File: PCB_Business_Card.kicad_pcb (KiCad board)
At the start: 2 copper layers, 88.9 x 50.8 mm, 6 parts, among them U1 NT3H1101W0FTTJ

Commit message: Updated Render
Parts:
- added G***: LOGO, LOGO, F.Cu at (114.1, 89.0)
- added G***: LOGO, LOGO, F.Cu at (161.5, 90.6)
- moved REF** 3.34 mm to (114.1, 89.0)
- moved C1 3.34 mm to (145.6, 90.6)
- moved D1 3.34 mm to (146.5, 93.2)
- moved R1 3.34 mm to (147.3, 90.6)
- moved U1 3.34 mm to (141.1, 89.5)
- moved ? 3.34 mm to (145.9, 88.5)
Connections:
- REF** pad : (no net) -> Net-(U1-LA)
- REF** pad 1: (no net) -> Net-(U1-LA)
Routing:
- net Net-(U1-LA): track 2.55 -> 22.0 mm
- net Net-(D1-K): track 0.00 -> 14.9 mm
- added copper zone on B.Cu, net (none)
- added copper zone on F.Cu, net (none)
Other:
- board text added: "linkedin.com/in/rahim-aziz"
- board text removed: "azizr6@mcmaster.ca"

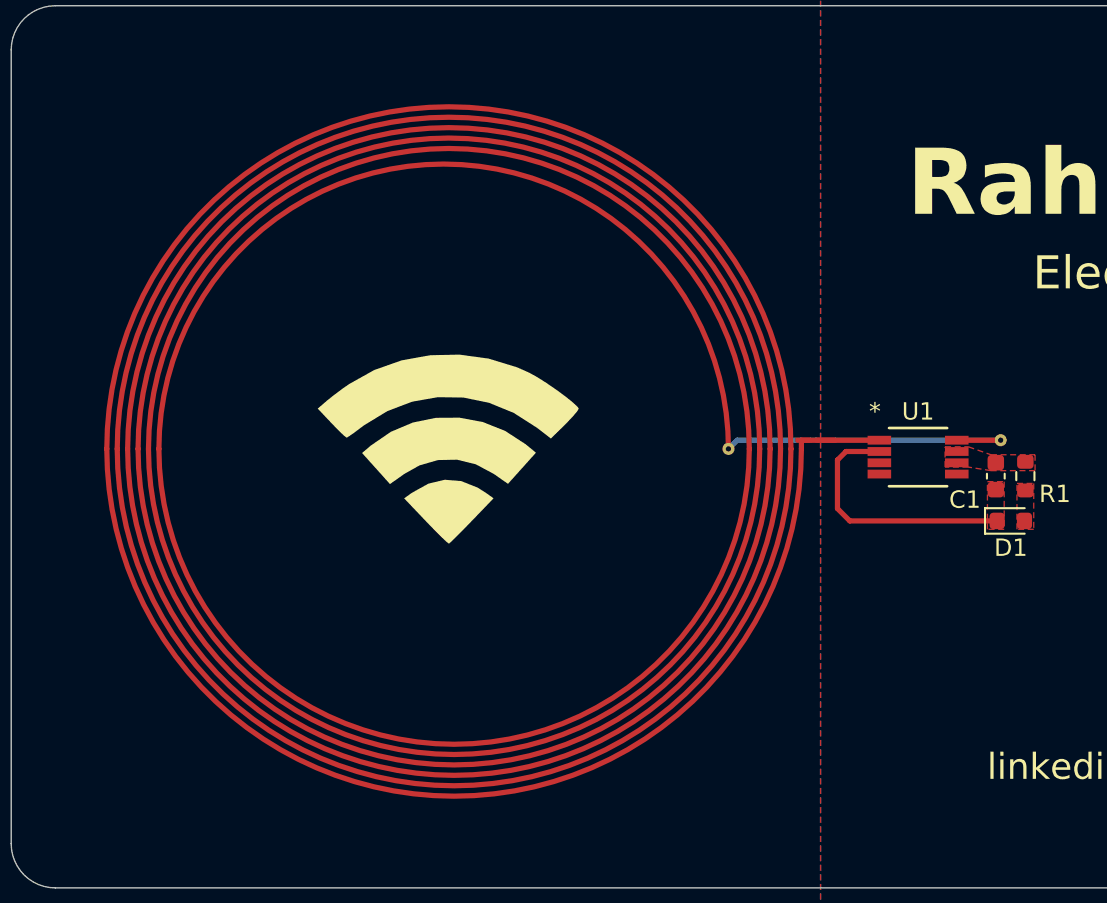
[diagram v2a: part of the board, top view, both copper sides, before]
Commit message: Added tuning capacitor
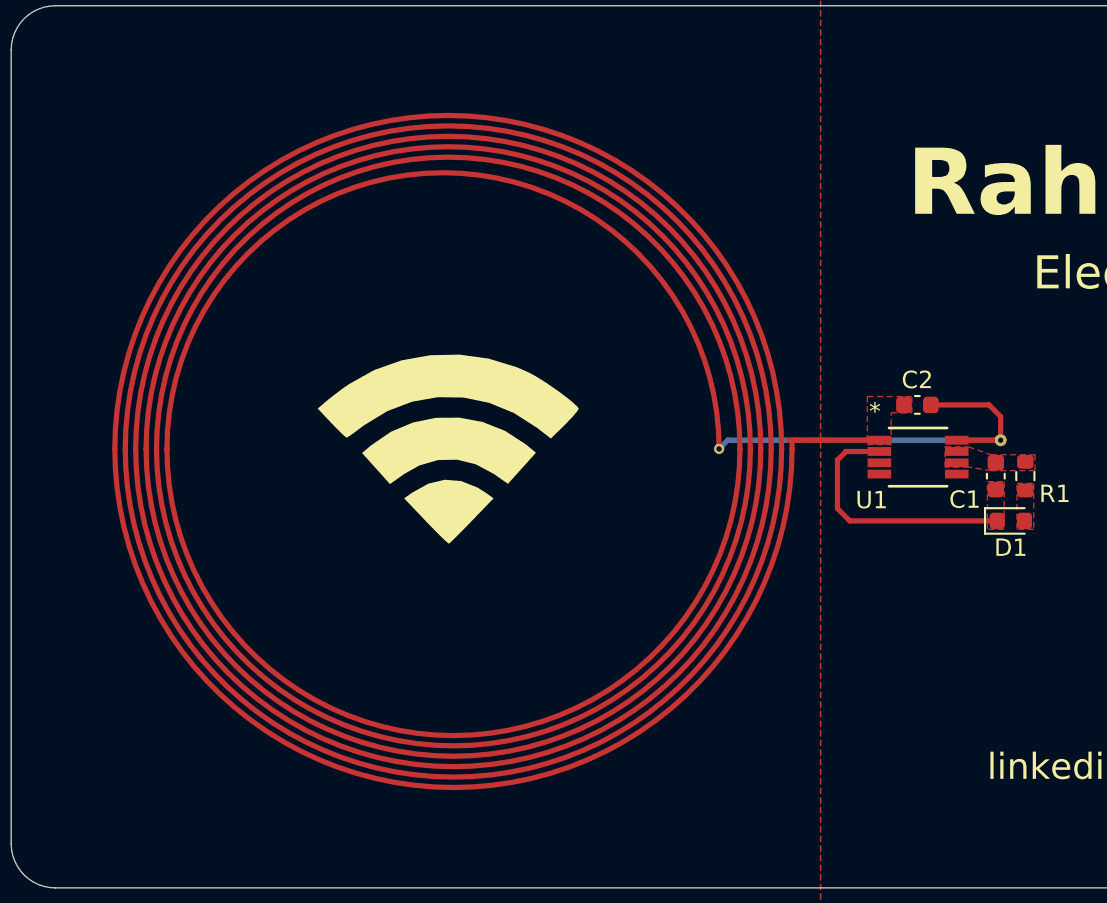
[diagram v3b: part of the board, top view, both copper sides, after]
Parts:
- added C2: 2p, Capacitor_SMD:C_0603_1608Metric, F.Cu at (141.1, 86.5)
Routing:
- net Net-(U1-LA): track 22.0 -> 28.7 mm
- added copper zone on F.Cu, net Net-(U1-LA)
